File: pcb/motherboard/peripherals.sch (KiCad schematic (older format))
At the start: 14 parts, among them J7 HEADER-1x04, J8 USB-A, U5 LM3526M-L, U6 MCP9804

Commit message: Changed crystal location for PCM2704
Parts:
- added C28: 100nF, SMT:C-0603, symbol CAP
- L3: value INDUCTOR -> 1A
- U5: value LM3526M-L -> LM3526M-H; symbol LM3526 -> LM3526-H
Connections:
- net +5V: now also C28.1
- net GND: now also C28.2
- no-connect marks 0 -> 1
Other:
- moved on the sheet: R15, R16, R17, R18
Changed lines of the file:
@@
 $EndComp
 $Comp
-L GND #PWR060
+L GND #PWR061
 U 1 1 54FEA8D3
 P 8900 2950
-F 0 "#PWR060" H 8900 3000 30  0001 C CNN
+F 0 "#PWR061" H 8900 3000 30  0001 C CNN
 F 1 "GND" H 8900 2825 30  0001 C CNN
 F 2 "" H 8900 2950 60  0000 C CNN
@@
 $EndComp
 $Comp
-L GNDPWR #PWR061
-U 1 1 54FEA8E9
-P 9100 2950
-F 0 "#PWR061" H 9100 3000 30  0001 C CNN
-F 1 "GNDPWR" H 9100 2825 30  0001 C CNN
-F 2 "" H 9100 2900 60  0000 C CNN
-F 3 "" H 9100 2900 60  0000 C CNN
-	1    9100 2950
-	1    0    0    -1
-$EndComp
-$Comp
-L LM3526 U5
+L LM3526-H U5
 U 1 1 54FF71F9
 P 4500 2500
 F 0 "U5" H 4150 3050 60  0000 L BNB
-F 1 "LM3526M-L" H 4150 1950 40  0000 L TNN
+F 1 "LM3526M-H" H 4150 1950 40  0000 L TNN
 F 2 "SMT-SOIC:8" H 4150 1850 40  0001 L CNN
 F 3 "" H 3750 2000 60  0001 C CNN
@@
 L +5V #PWR062
 U 1 1 54FF739C
-P 3800 1950
-F 0 "#PWR062" H 3800 2175 30  0001 C CNN
-F 1 "+5V" V 3725 1950 30  0001 C CNN
-F 2 "" H 3800 1950 60  0000 C CNN
-F 3 "" H 3800 1950 60  0000 C CNN
-	1    3800 1950
+P 3800 1700
+F 0 "#PWR062" H 3800 1925 30  0001 C CNN
+F 1 "+5V" V 3725 1700 30  0001 C CNN
+F 2 "" H 3800 1700 60  0000 C CNN
+F 3 "" H 3800 1700 60  0000 C CNN
+	1    3800 1700
 	1    0    0    -1
 $EndComp
@@
 	1    0    0    -1
 $EndComp
-Text HLabel 2150 2300 0    50   Input ~ 0
+Text HLabel 1600 2300 0    50   Input ~ 0
 USB-EN1
-Text HLabel 2150 2600 0    50   Output ~ 0
+Text HLabel 1600 2600 0    50   Output ~ 0
 USB-EN2
-Text HLabel 2150 2400 0    50   Input ~ 0
+Text HLabel 1600 2400 0    50   Input ~ 0
 USB-FLAG1
-Text HLabel 2150 2700 0    50   Output ~ 0
+Text HLabel 1600 2700 0    50   Output ~ 0
 USB-FLAG2
 $Comp
@@
 P 6350 2300
 F 0 "L3" H 6350 2390 60  0000 C CNB
-F 1 "INDUCTOR" H 6350 2230 40  0000 C CNN
+F 1 "1A" H 6350 2230 40  0000 C CNN
 F 2 "SMT:FER-0805" H 6350 2170 40  0001 C CNN
 F 3 "" H 6350 2400 60  0000 C CNN
@@
 	8900 2600 8900 2950
 Wire Wire Line
-	3800 1950 3800 2100
+	3800 1700 3800 2100
 Wire Wire Line
 	3800 2100 4050 2100
@@
 	3800 2900 3800 3100
 Wire Wire Line
-	2150 2300 4050 2300
-Wire Wire Line
-	2150 2400 4050 2400
-Wire Wire Line
-	2150 2600 4050 2600
-Wire Wire Line
-	2150 2700 4050 2700
+	1600 2300 4050 2300
+Wire Wire Line
+	1600 2400 4050 2400
+Wire Wire Line
+	1600 2600 4050 2600
+Wire Wire Line
+	1600 2700 4050 2700
 Wire Wire Line
 	4950 2700 5250 2700
@@
 Wire Wire Line
 	7450 2400 9200 2400
-Wire Wire Line
-	6450 2300 9200 2300
 Wire Wire Line
 	4950 2300 6250 2300
@@
 L RESISTOR R15
 U 1 1 5508343F
-P 2550 2000
-F 0 "R15" H 2550 2085 60  0000 C CNB
-F 1 "100k" H 2550 1925 40  0000 C CNN
-F 2 "SMT:R-0603" H 2550 1860 40  0001 C CNN
-F 3 "" H 2550 2100 60  0000 C CNN
-F 4 "-" H 2550 2160 45  0001 C CNN "Part"
-	1    2550 2000
+P 2000 2000
+F 0 "R15" H 2000 2085 60  0000 C CNB
+F 1 "100k" H 2000 1925 40  0000 C CNN
+F 2 "SMT:R-0603" H 2000 1860 40  0001 C CNN
+F 3 "" H 2000 2100 60  0000 C CNN
+F 4 "-" H 2000 2160 45  0001 C CNN "Part"
+	1    2000 2000
 	0    -1   -1   0
 $EndComp
@@
 L RESISTOR R16
 U 1 1 550834AC
-P 2850 2000
-F 0 "R16" H 2850 2085 60  0000 C CNB
-F 1 "100k" H 2850 1925 40  0000 C CNN
-F 2 "SMT:R-0603" H 2850 1860 40  0001 C CNN
-F 3 "" H 2850 2100 60  0000 C CNN
-F 4 "-" H 2850 2160 45  0001 C CNN "Part"
-	1    2850 2000
+P 2300 2000
+F 0 "R16" H 2300 2085 60  0000 C CNB
+F 1 "100k" H 2300 1925 40  0000 C CNN
+F 2 "SMT:R-0603" H 2300 1860 40  0001 C CNN
+F 3 "" H 2300 2100 60  0000 C CNN
+F 4 "-" H 2300 2160 45  0001 C CNN "Part"
+	1    2300 2000
 	0    -1   -1   0
 $EndComp
@@
 L RESISTOR R17
 U 1 1 550834E4
-P 3150 2000
-F 0 "R17" H 3150 2085 60  0000 C CNB
-F 1 "100k" H 3150 1925 40  0000 C CNN
-F 2 "SMT:R-0603" H 3150 1860 40  0001 C CNN
-F 3 "" H 3150 2100 60  0000 C CNN
-F 4 "-" H 3150 2160 45  0001 C CNN "Part"
-	1    3150 2000
+P 2600 2000
+F 0 "R17" H 2600 2085 60  0000 C CNB
+F 1 "100k" H 2600 1925 40  0000 C CNN
+F 2 "SMT:R-0603" H 2600 1860 40  0001 C CNN
+F 3 "" H 2600 2100 60  0000 C CNN
+F 4 "-" H 2600 2160 45  0001 C CNN "Part"
+	1    2600 2000
 	0    -1   -1   0
 $EndComp
@@
 L RESISTOR R18
 U 1 1 5508351A
-P 3450 2000
-F 0 "R18" H 3450 2085 60  0000 C CNB
-F 1 "100k" H 3450 1925 40  0000 C CNN
-F 2 "SMT:R-0603" H 3450 1860 40  0001 C CNN
-F 3 "" H 3450 2100 60  0000 C CNN
-F 4 "-" H 3450 2160 45  0001 C CNN "Part"
-	1    3450 2000
-	0    -1   -1   0
-$EndComp
-Wire Wire Line
-	2550 2100 2550 2300
-Connection ~ 2550 2300
-Wire Wire Line
-	2850 2100 2850 2400
-Connection ~ 2850 2400
-Wire Wire Line
-	3150 2100 3150 2600
-Connection ~ 3150 2600
-Wire Wire Line
-	3450 2100 3450 2700
-Connection ~ 3450 2700
+P 2900 2000
+F 0 "R18" H 2900 2085 60  0000 C CNB
+F 1 "100k" H 2900 1925 40  0000 C CNN
+F 2 "SMT:R-0603" H 2900 1860 40  0001 C CNN
+F 3 "" H 2900 2100 60  0000 C CNN
+F 4 "-" H 2900 2160 45  0001 C CNN "Part"
+	1    2900 2000
+	0    -1   -1   0
+$EndComp
+Wire Wire Line
+	2000 2100 2000 2300
+Connection ~ 2000 2300
+Wire Wire Line
+	2300 2100 2300 2400
+Connection ~ 2300 2400
+Wire Wire Line
+	2600 2100 2600 2600
+Connection ~ 2600 2600
+Wire Wire Line
+	2900 2100 2900 2700
+Connection ~ 2900 2700
 $Comp
 L +3V3 #PWR073
 U 1 1 55083A62
-P 3000 1700
-F 0 "#PWR073" H 3000 1925 30  0001 C CNN
-F 1 "+3V3" V 2925 1700 30  0001 C CNN
-F 2 "" H 3000 1700 60  0000 C CNN
-F 3 "" H 3000 1700 60  0000 C CNN
-	1    3000 1700
-	1    0    0    -1
-$EndComp
-Wire Wire Line
-	3000 1800 3000 1700
-Wire Wire Line
-	2550 1800 3450 1800
-Wire Wire Line
-	2850 1800 2850 1900
-Wire Wire Line
-	2550 1800 2550 1900
-Connection ~ 2850 1800
-Wire Wire Line
-	3150 1800 3150 1900
-Connection ~ 3000 1800
-Wire Wire Line
-	3450 1800 3450 1900
-Connection ~ 3150 1800
+P 2450 1700
+F 0 "#PWR073" H 2450 1925 30  0001 C CNN
+F 1 "+3V3" V 2375 1700 30  0001 C CNN
+F 2 "" H 2450 1700 60  0000 C CNN
+F 3 "" H 2450 1700 60  0000 C CNN
+	1    2450 1700
+	1    0    0    -1
+$EndComp
+Wire Wire Line
+	2450 1800 2450 1700
+Wire Wire Line
+	2000 1800 2900 1800
+Wire Wire Line
+	2300 1800 2300 1900
+Wire Wire Line
+	2000 1800 2000 1900
+Connection ~ 2300 1800
+Wire Wire Line
+	2600 1800 2600 1900
+Connection ~ 2450 1800
+Wire Wire Line
+	2900 1800 2900 1900
+Connection ~ 2600 1800
+NoConn ~ 3800 5950
+$Comp
+L PWR_FLAG #FLG1
+U 1 1 550C9F1A
+P 9050 2300
+F 0 "#FLG1" H 9050 2600 60  0001 C CNN
+F 1 "PWR_FLAG" H 9050 2250 40  0001 C CNN
+F 2 "" H 8950 2500 60  0001 C CNN
+F 3 "" H 9050 2600 60  0001 C CNN
+	1    9050 2300
+	1    0    0    -1
+$EndComp
+Wire Wire Line
+	6450 2300 9200 2300
+Connection ~ 9050 2300
+$Comp
+L GNDPWR #PWR074
+U 1 1 550E11E4
+P 9100 2950
+F 0 "#PWR074" H 9100 3000 30  0001 C CNN
+F 1 "GNDPWR" H 9100 2825 30  0001 C CNN
+F 2 "" H 9100 2900 60  0000 C CNN
+F 3 "" H 9100 2900 60  0000 C CNN
+	1    9100 2950
+	1    0    0    -1
+$EndComp
+$Comp
+L CAP C28
+U 1 1 5520745D
+P 3500 1850
+F 0 "C28" H 3530 1940 60  0000 L CNB
+F 1 "100nF" H 3530 1760 45  0000 L CNN
+F 2 "SMT:C-0603" H 3535 1695 40  0001 L CNN
+F 3 "" H 3500 1950 60  0001 C CNN
+F 4 "-" H 3540 2015 45  0001 L CNN "Part"
+	1    3500 1850
+	0    -1   -1   0
+$EndComp
+Wire Wire Line
+	3600 1850 3800 1850
+Connection ~ 3800 1850
+$Comp
+L GND #PWR075
+U 1 1 55207785
+P 3300 2000
+F 0 "#PWR075" H 3300 2050 30  0001 C CNN
+F 1 "GND" H 3300 1875 30  0001 C CNN
+F 2 "" H 3300 2000 60  0000 C CNN
+F 3 "" H 3300 2000 60  0000 C CNN
+	1    3300 2000
+	1    0    0    -1
+$EndComp
+Wire Wire Line
+	3400 1850 3300 1850
+Wire Wire Line
+	3300 1850 3300 2000
 $EndSCHEMATC

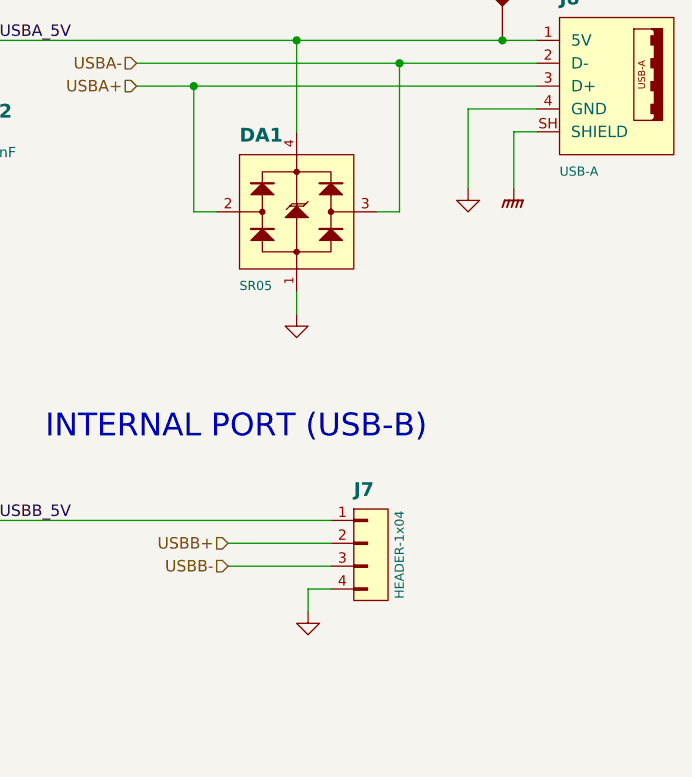
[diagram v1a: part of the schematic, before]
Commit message: Tidy up motherboard schematic
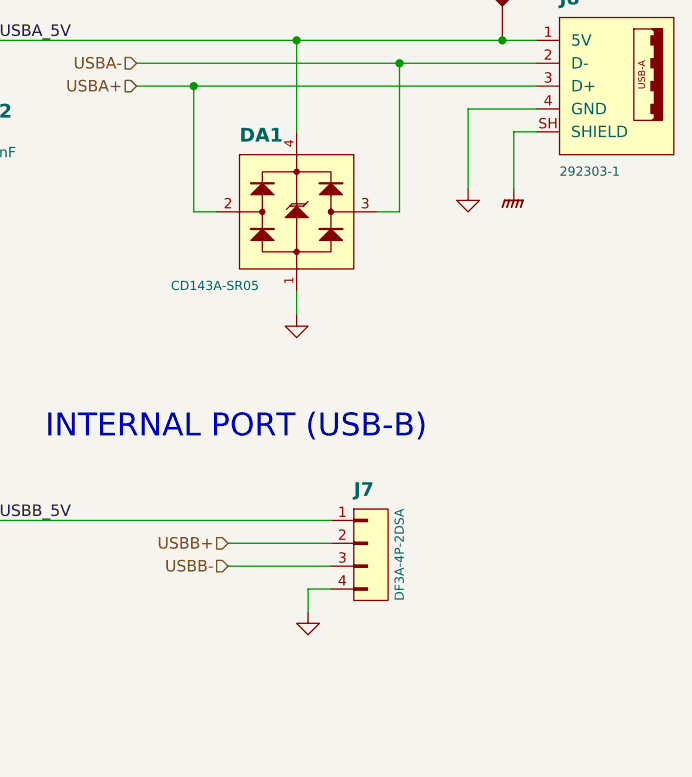
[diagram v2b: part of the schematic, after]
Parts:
- C10, C11, C12, C13, C28, L3, R15, R16, R17, R18: Family (none) -> Passive
- DA1: value SR05 -> CD143A-SR05; Family (none) -> Passive; MFG (none) -> Bourns
- J7: value HEADER-1x04 -> DF3A-4P-2DSA; Family (none) -> Connector; MFG (none) -> Hirose
- J8: value USB-A -> 292303-1; Family (none) -> Connector; MFG (none) -> TE Connectivity
- U5, U6: Family (none) -> IC
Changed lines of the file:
@@
 Sheet 4 4
 Title "MOTHERBOARD\\nPERIPHERALS"
-Date "Wed 18 Mar 2015"
+Date "Sun 12 Apr 2015"
 Rev "A"
 Comp ""
@@
 P 9550 2500
 F 0 "J8" H 9300 2850 60  0000 L BNB
-F 1 "USB-A" H 9300 2150 40  0000 L TNN
+F 1 "292303-1" H 9300 2150 40  0000 L TNN
 F 2 "Conn-IO:USBA-TE-292303-1" H 9300 2075 40  0001 L TNN
 F 3 "" H 9300 2800 60  0000 C CNN
+F 4 "Connector" H 9550 2500 60  0001 C CNN "Family"
+F 5 "TE Connectivity" H 9550 2500 60  0001 C CNN "MFG"
 	1    9550 2500
 	1    0    0    -1
@@
 P 8450 4550
 F 0 "J7" H 8400 4800 60  0000 L BNB
-F 1 "HEADER-1x04" V 8600 4550 40  0000 C CNN
+F 1 "DF3A-4P-2DSA" V 8600 4550 40  0000 C CNN
 F 2 "Conn-Hirose:DF3A-4P-2DSA" H 8450 4550 60  0001 C CNN
 F 3 "" H 8450 4550 60  0001 C CNN
+F 4 "Connector" H 8450 4550 60  0001 C CNN "Family"
+F 5 "Hirose" H 8450 4550 60  0001 C CNN "MFG"
 	1    8450 4550
 	1    0    0    -1
@@
 F 2 "SMT-SOIC:8" H 4150 1850 40  0001 L CNN
 F 3 "" H 3750 2000 60  0001 C CNN
+F 4 "IC" H 4500 2500 60  0001 C CNN "Family"
 	1    4500 2500
 	1    0    0    -1
@@
 F 3 "" H 6350 2400 60  0000 C CNN
 F 4 "-" H 6350 2465 45  0001 C CNN "PART"
+F 5 "Passive" H 6350 2300 60  0001 C CNN "Family"
 	1    6350 2300
 	1    0    0    -1
@@
 F 3 "" H 5550 2800 60  0001 C CNN
 F 4 "-" H 5590 2865 45  0001 L CNN "Part"
+F 5 "Passive" H 5550 2700 60  0001 C CNN "Family"
 	1    5550 2700
 	1    0    0    -1
@@
 F 3 "" H 6000 2800 60  0001 C CNN
 F 4 "-" H 6040 2865 45  0001 L CNN "Part"
+F 5 "Passive" H 6000 2700 60  0001 C CNN "Family"
 	1    6000 2700
 	1    0    0    -1
@@
 F 3 "" H 6700 2800 60  0001 C CNN
 F 4 "-" H 6740 2865 45  0001 L CNN "Part"
+F 5 "Passive" H 6700 2700 60  0001 C CNN "Family"
 	1    6700 2700
 	1    0    0    -1
@@
 F 3 "" H 2600 5750 60  0001 C CNN
 F 4 "-" H 2640 5815 45  0001 L CNN "Part"
+F 5 "Passive" H 2600 5650 60  0001 C CNN "Family"
 	1    2600 5650
 	0    -1   -1   0
@@
 F 2 "SMT-SOP:MSOP8" H 3050 5725 40  0001 L TNN
 F 3 "" H 3050 6600 50  0000 C CNN
+F 4 "IC" H 3400 6200 60  0001 C CNN "Family"
 	1    3400 6200
 	1    0    0    -1
@@
 P 8150 3050
 F 0 "DA1" H 7900 3350 60  0000 L BNB
-F 1 "SR05" H 7900 2750 40  0000 L TNN
+F 1 "CD143A-SR05" H 7600 2750 40  0000 L TNN
 F 2 "SMT-SOT:SOT-143" H 7900 2675 40  0001 L TNN
 F 3 "" H 8000 3170 60  0000 C CNN
+F 4 "Passive" H 8150 3050 60  0001 C CNN "Family"
+F 5 "Bourns" H 8150 3050 60  0001 C CNN "MFG"
 	1    8150 3050
 	1    0    0    -1
@@
 F 3 "" H 2000 2100 60  0000 C CNN
 F 4 "-" H 2000 2160 45  0001 C CNN "Part"
+F 5 "Passive" H 2000 2000 60  0001 C CNN "Family"
 	1    2000 2000
 	0    -1   -1   0
@@
 F 3 "" H 2300 2100 60  0000 C CNN
 F 4 "-" H 2300 2160 45  0001 C CNN "Part"
+F 5 "Passive" H 2300 2000 60  0001 C CNN "Family"
 	1    2300 2000
 	0    -1   -1   0
@@
 F 3 "" H 2600 2100 60  0000 C CNN
 F 4 "-" H 2600 2160 45  0001 C CNN "Part"
+F 5 "Passive" H 2600 2000 60  0001 C CNN "Family"
 	1    2600 2000
 	0    -1   -1   0
@@
 F 3 "" H 2900 2100 60  0000 C CNN
 F 4 "-" H 2900 2160 45  0001 C CNN "Part"
+F 5 "Passive" H 2900 2000 60  0001 C CNN "Family"
 	1    2900 2000
 	0    -1   -1   0
@@
 F 3 "" H 3500 1950 60  0001 C CNN
 F 4 "-" H 3540 2015 45  0001 L CNN "Part"
+F 5 "Passive" H 3500 1850 60  0001 C CNN "Family"
 	1    3500 1850
 	0    -1   -1   0
